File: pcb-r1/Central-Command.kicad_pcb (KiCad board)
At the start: 4 copper layers, 38.1 x 63.5 mm, 50 parts, among them P101 CONN_01X10, P102 CONN_01X10, P103 CONN_01X04, P104 CONN_01X02, P105 CONN_01X04, P106 CONN_01X02, P201 CONN_01X06, P202 CONN_01X04, P203 CONN_01X04, P204 CONN_01X03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

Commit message: Intermediate save of the layout
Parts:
- added C104: 0.1μF, Capacitors_SMD:C_0805, B.Cu at (93.5, 90.6)
- added C105: 1μF, Capacitors_SMD:C_1206, B.Cu at (95.8, 90.0)
- added C106: 10μF, Capacitors_SMD:C_1206, B.Cu at (98.3, 90.0)
- added C107: 0.1μF, Capacitors_SMD:C_0805, B.Cu at (98.3, 106.6)
- added C108: 1μF, Capacitors_SMD:C_1206, B.Cu at (95.9, 107.1)
- added C109: 10μF, Capacitors_SMD:C_1206, B.Cu at (93.4, 107.1)
- added R206: 0Ω, Resistors_SMD:R_0805, B.Cu at (81.9, 117.3)
- added R207: 0Ω, Resistors_SMD:R_0805, B.Cu at (81.9, 115.2)
- added R208: 0Ω, Resistors_SMD:R_0805, B.Cu at (81.9, 113.0)
- added R209: 0Ω, Resistors_SMD:R_0805, B.Cu at (81.9, 110.9)
- C101, C102, C103, C201, C301, C304, C305, C306, R201, R202, R203, R204, R205, R301, R302, R303, R304, R305, R306, R307: moved to B.Cu
- P302: value CONN_01X02 -> ALT PWR
- moved P205 32.6 mm to (112.1, 118.1)
- moved R303 21.5 mm to (82.2, 122.9), turned to 270 degrees
- moved R302 21.5 mm to (79.8, 122.9), turned to 270 degrees
- moved P302 17.1 mm to (96.8, 137.7), turned to 90 degrees
- moved R205 16.4 mm to (108.5, 118.1), turned to 0 degrees
- moved C301 13.6 mm to (83.6, 132.1), turned to 0 degrees
- moved D301 13.0 mm to (98.8, 133.3), turned to 0 degrees
- moved P105 12.6 mm to (112.1, 124.3)
- moved P202 12.5 mm to (84.6, 117.5)
- moved R301 12.4 mm to (90.4, 118.9), turned to 90 degrees
- moved P104 11.7 mm to (112.1, 111.9)
- moved C103 11.2 mm to (83.4, 91.1), turned to 0 degrees
- moved L101 10.4 mm to (90.8, 92.7), turned to 225 degrees
- moved C201 9.51 mm to (95.2, 116.1)
- moved R307 8.87 mm to (93.3, 125.6)
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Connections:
- net Net-(C302-Pad1) renamed /Power/VCCIO
- P103 pad 3: (no net) -> /SPI_MISO
- P103 pad 4: (no net) -> /SPI_MOSI
- P104 pad 2: (no net) -> /I2C1_SCK
- P203 pad 1: /Comm/SDA -> Net-(P203-Pad1)
- P203 pad 2: /Comm/SCL -> Net-(P203-Pad2)
- P203 pad 3: /Comm/PWR -> Net-(P203-Pad3)
- P203 pad 4: GND -> Net-(P203-Pad4)
- P301 pad 4: (no net) -> Net-(P301-Pad4)
- R204 pad 1: (no net) -> /Comm/TRACE
- R301 pad 2: (no net) -> /Comm/NRST
- SW201 pad 2: /Comm/NRST -> GND
- U101 pad 36: (no net) -> /I2C1_SCK
- U101 pad 40: (no net) -> /SPI1_MISO
- U101 pad 41: (no net) -> /SPI1_MOSI
- U301 pad 10: (no net) -> Net-(U301-Pad10)
- U301 pad 11: (no net) -> Net-(U301-Pad11)
- U301 pad 12: (no net) -> Net-(U301-Pad12)
- U301 pad 13: (no net) -> Net-(U301-Pad13)
- U301 pad 23: (no net) -> Net-(U301-Pad23)
- U301 pad 25: (no net) -> Net-(U301-Pad25)
- U301 pad 27: (no net) -> Net-(U301-Pad27)
- U301 pad 28: (no net) -> Net-(U301-Pad28)
- U301 pad 29: (no net) -> Net-(U301-Pad29)
- U301 pad 3: (no net) -> Net-(U301-Pad3)
- U301 pad 31: (no net) -> Net-(U301-Pad31)
- U301 pad 33: (no net) -> GND
- U301 pad 5: (no net) -> Net-(U301-Pad5)
- U301 pad 6: (no net) -> Net-(U301-Pad6)
- U301 pad 7: (no net) -> Net-(U301-Pad7)
- U301 pad 9: (no net) -> Net-(U301-Pad9)
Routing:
- net GND: track 0.00 -> 89.0 mm, vias 0 -> 15
- net /Power/VCCIO: track 0.00 -> 43.9 mm, vias 0 -> 3
- net /Comm/PWR: track 0.00 -> 37.7 mm, vias 0 -> 6
- net Net-(C305-Pad1): track 0.00 -> 21.5 mm, vias 0 -> 1
- net /Comm/BOOT0: track 0.00 -> 15.0 mm
- net Net-(P301-Pad2): track 0.00 -> 13.3 mm
- net Net-(R301-Pad1): track 0.00 -> 9.33 mm, vias 0 -> 1
- net Net-(C301-Pad1): track 0.00 -> 8.57 mm, vias 0 -> 1
- net Net-(P301-Pad3): track 0.00 -> 8.32 mm
- net Net-(C101-Pad1): track 0.00 -> 7.80 mm, vias 0 -> 1
- net Net-(D301-Pad2): track 0.00 -> 7.18 mm
- net /Comm/NRST: track 0.00 -> 6.92 mm, vias 0 -> 1
- net Net-(R305-Pad2): track 0.00 -> 4.84 mm, vias 0 -> 1
- net Net-(C304-Pad1): track 0.00 -> 3.87 mm, vias 0 -> 1
- net Net-(R304-Pad2): track 0.00 -> 3.53 mm, vias 0 -> 1
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- added copper zone on PWR, net /Comm/PWR
- added copper zone on GND, net GND

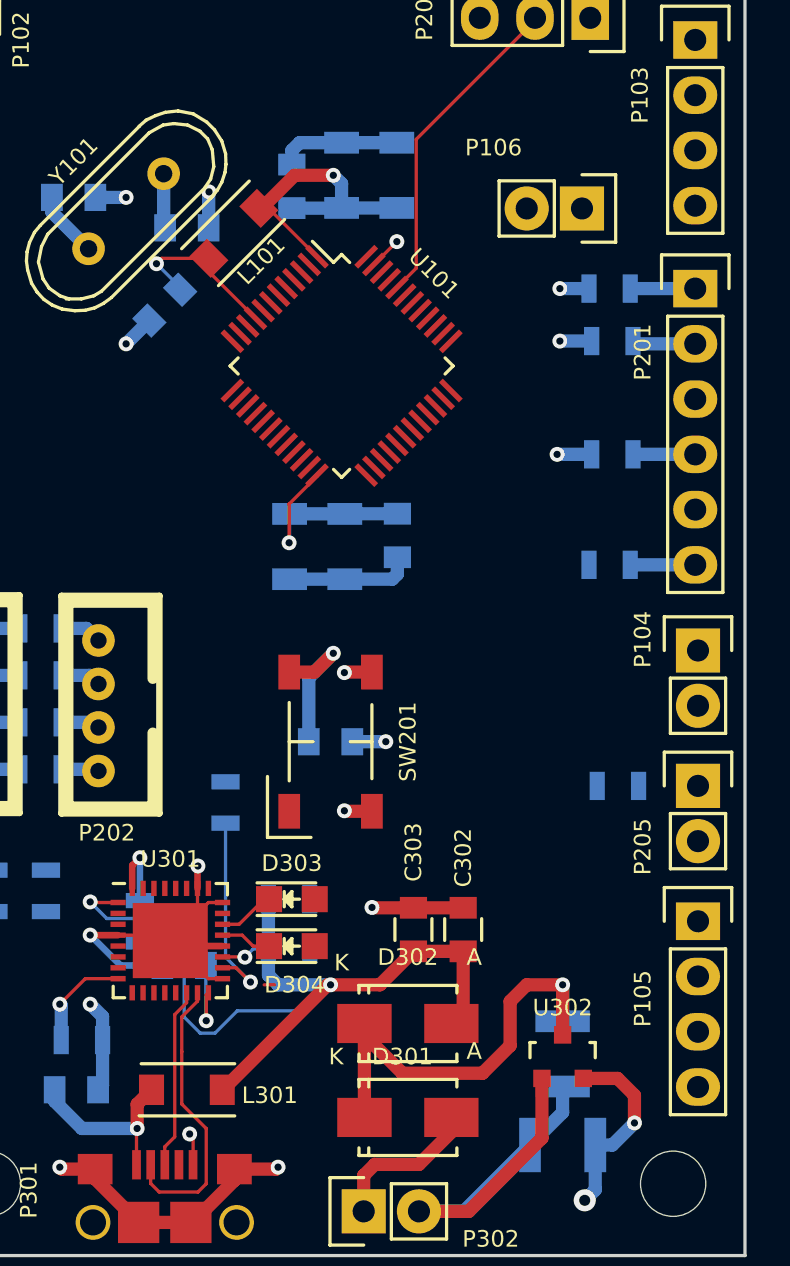
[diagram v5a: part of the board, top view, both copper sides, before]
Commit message: Started the basic layout.
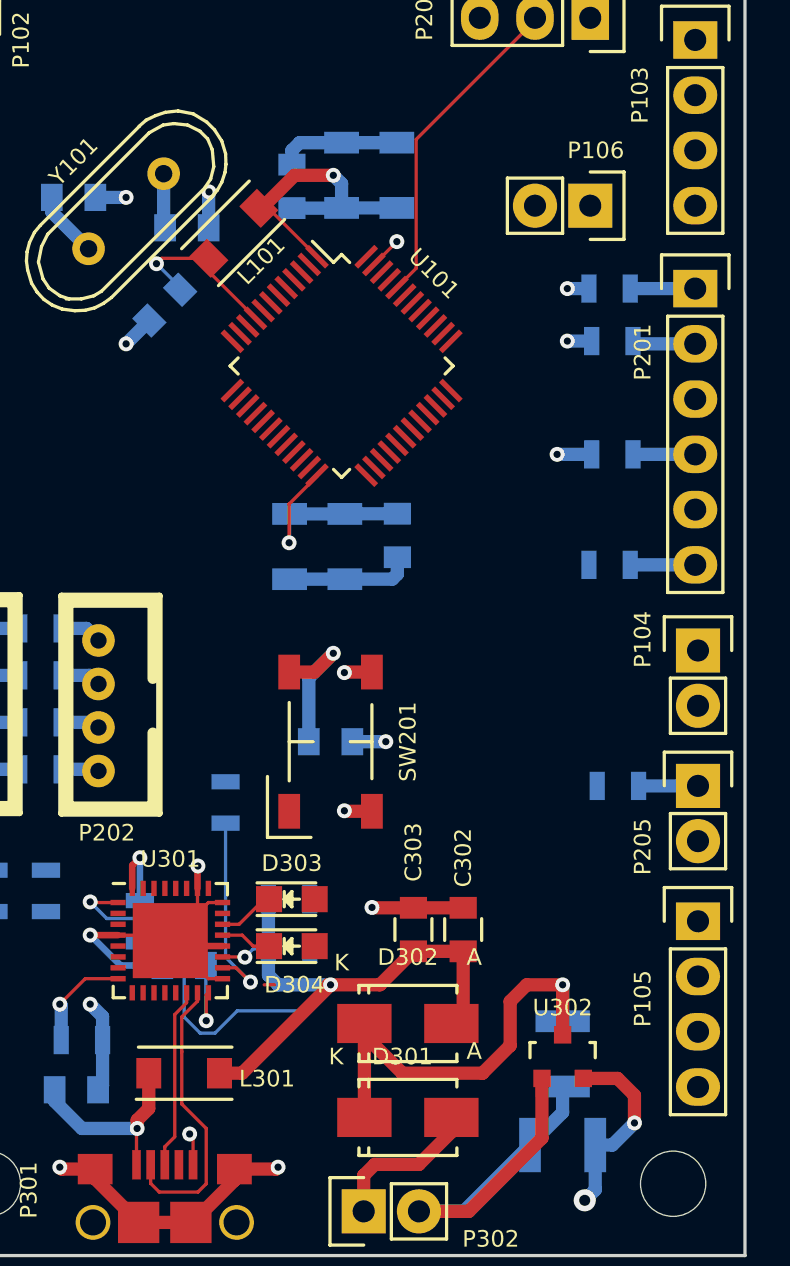
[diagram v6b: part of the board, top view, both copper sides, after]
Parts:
- moved L301 0.77 mm to (88.5, 131.3)
- moved P106 0.40 mm to (107.2, 91.4)
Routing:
- net Net-(P205-Pad1): track 0.00 -> 2.73 mm
- net Net-(C301-Pad1): track 8.57 -> 9.28 mm
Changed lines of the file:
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@@
   (general
     (links 145)
-    (no_connects 55)
-    (area 76.124999 76.124999 114.375001 139.775001)
+    (no_connects 54)
+    (area 74.587101 74.3331 117.711947 142.14856)
     (thickness 1.6)
     (drawings 4)
-    (tracks 254)
+    (tracks 256)
     (zones 0)
     (modules 60)
@@
   )
   (setup
-    (last_trace_width 0.6096)
+    (last_trace_width 0.1524)
     (user_trace_width 0.3048)
     (user_trace_width 0.6096)
@@
   )
   (module Inductors_NEOSID:Neosid_Inductor_SM1206 (layer F.Cu)
-    (at 88.646 132.08)
+    (at 88.519 131.318)
     (descr "Neosid, Inductor, SM1206, Festinduktivitaet, SMD,")
     (tags "Neosid, Inductor, SM1206, Festinduktivitaet, SMD,")
@@
   )
   (module Pin_Headers:Pin_Header_Straight_1x02 (layer F.Cu)
-    (at 106.807 91.567 270)
+    (at 107.188 91.44 270)
     (descr "Through hole pin header")
     (tags "pin header")
-    (fp_text reference P106 (at -2.794 4.064 360) (layer F.SilkS)
+    (fp_text reference P106 (at -2.54 -0.254 360) (layer F.SilkS)
       (effects (font (size 0.762 0.762) (thickness 0.127)))
     )
@@
   (segment (start 89.655527 93.859473) (end 89.655527 94.471294) (width 0.1524) (layer F.Cu) (net 1))
   (segment (start 89.655527 94.471294) (end 91.798202 96.613969) (width 0.1524) (layer F.Cu) (net 1))
-  (segment (start 107.254 97.663) (end 105.791 97.663) (width 0.6096) (layer B.Cu) (net 2) (status 400000))
-  (via (at 105.791 97.663) (size 0.6858) (drill 0.3302) (layers F.Cu B.Cu) (net 2))
+  (via (at 106.133919 97.663) (size 0.6858) (drill 0.3302) (layers F.Cu B.Cu) (net 2))
+  (segment (start 107.254 97.663) (end 106.133919 97.663) (width 0.6096) (layer B.Cu) (net 2))
   (segment (start 96.25 116.078) (end 97.79 116.078) (width 0.6096) (layer B.Cu) (net 2))
   (via (at 97.79 116.078) (size 0.6858) (drill 0.3302) (layers F.Cu B.Cu) (net 2))
@@
   (via (at 95.377 112.014) (size 0.6858) (drill 0.3302) (layers F.Cu B.Cu) (net 5))
   (segment (start 94.25 113.141) (end 95.377 112.014) (width 0.6096) (layer B.Cu) (net 5))
+  (segment (start 86.36 133.858) (end 86.36 133.477) (width 0.6096) (layer F.Cu) (net 6))
+  (segment (start 86.8934 132.9436) (end 86.8934 131.318) (width 0.6096) (layer F.Cu) (net 6))
+  (segment (start 86.36 133.477) (end 86.8934 132.9436) (width 0.6096) (layer F.Cu) (net 6))
   (segment (start 82.566 132.08) (end 82.566 132.604) (width 0.6096) (layer B.Cu) (net 6))
   (segment (start 82.566 132.604) (end 83.82 133.858) (width 0.6096) (layer B.Cu) (net 6))
   (segment (start 83.82 133.858) (end 86.36 133.858) (width 0.6096) (layer B.Cu) (net 6))
   (via (at 86.36 133.858) (size 0.6858) (drill 0.3302) (layers F.Cu B.Cu) (net 6))
-  (segment (start 86.36 133.858) (end 86.36 132.7404) (width 0.6096) (layer F.Cu) (net 6))
-  (segment (start 86.36 132.7404) (end 87.0204 132.08) (width 0.6096) (layer F.Cu) (net 6))
   (segment (start 86.33 133.888) (end 86.33 135.526) (width 0.1524) (layer F.Cu) (net 6))
   (segment (start 86.36 133.858) (end 86.33 133.888) (width 0.1524) (layer F.Cu) (net 6))
@@
   (via (at 105.918 127.254) (size 0.6858) (drill 0.3302) (layers F.Cu B.Cu) (net 8))
   (segment (start 96.80702 133.35) (end 96.80702 129.032) (width 0.6096) (layer F.Cu) (net 8))
-  (segment (start 107.254 102.87) (end 105.664 102.87) (width 0.6096) (layer B.Cu) (net 9) (status 400000))
+  (via (at 106.133919 95.25) (size 0.6858) (drill 0.3302) (layers F.Cu B.Cu) (net 9))
+  (segment (start 107.127 95.25) (end 106.133919 95.25) (width 0.6096) (layer B.Cu) (net 9))
+  (segment (start 107.254 102.87) (end 105.664 102.87) (width 0.6096) (layer B.Cu) (net 9))
   (via (at 105.664 102.87) (size 0.6858) (drill 0.3302) (layers F.Cu B.Cu) (net 9))
   (segment (start 91.954473 91.560527) (end 92.081473 91.560527) (width 0.6096) (layer F.Cu) (net 9))
@@
   (segment (start 91.954473 91.560527) (end 92.401614 91.560527) (width 0.1524) (layer F.Cu) (net 9))
   (segment (start 92.401614 91.560527) (end 94.626629 93.785542) (width 0.1524) (layer F.Cu) (net 9))
-  (segment (start 107.127 95.25) (end 105.791 95.25) (width 0.6096) (layer B.Cu) (net 9))
-  (via (at 105.791 95.25) (size 0.6858) (drill 0.3302) (layers F.Cu B.Cu) (net 9))
   (segment (start 82.865 115.189) (end 84.346 115.189) (width 0.6096) (layer B.Cu) (net 9))
   (segment (start 84.346 115.189) (end 84.582 115.425) (width 0.6096) (layer B.Cu) (net 9))
@@
   (segment (start 112.014 97.79) (end 109.281 97.79) (width 0.6096) (layer B.Cu) (net 44))
   (segment (start 109.281 97.79) (end 109.154 97.663) (width 0.6096) (layer B.Cu) (net 44))
-  (segment (start 112.014 102.87) (end 109.154 102.87) (width 0.6096) (layer B.Cu) (net 45) (status C00000))
-  (segment (start 112.014 107.95) (end 109.027 107.95) (width 0.6096) (layer B.Cu) (net 46) (status C00000))
+  (segment (start 112.014 102.87) (end 109.154 102.87) (width 0.6096) (layer B.Cu) (net 45))
+  (segment (start 112.014 107.95) (end 109.027 107.95) (width 0.6096) (layer B.Cu) (net 46))
   (segment (start 82.865 113.03) (end 84.187 113.03) (width 0.6096) (layer B.Cu) (net 47))
   (segment (start 84.187 113.03) (end 84.582 113.425) (width 0.6096) (layer B.Cu) (net 47))
@@
   (segment (start 99.187 88.392) (end 99.187 94.316339) (width 0.1524) (layer F.Cu) (net 49))
   (segment (start 99.187 94.316339) (end 98.303584 95.199755) (width 0.1524) (layer F.Cu) (net 49))
+  (segment (start 112.141 118.11) (end 109.408 118.11) (width 0.6096) (layer B.Cu) (net 50))
   (segment (start 88.087189 134.241411) (end 87.63 134.6986) (width 0.1524) (layer F.Cu) (net 51))
   (segment (start 88.634 127.622) (end 88.634 128.076452) (width 0.1524) (layer F.Cu) (net 51))
@@
   (via (at 82.804 128.143) (size 0.6858) (drill 0.3302) (layers F.Cu B.Cu) (net 59))
   (segment (start 82.87 128.209) (end 82.804 128.143) (width 0.6096) (layer B.Cu) (net 59))
+  (segment (start 90.1446 131.318) (end 91.186 131.318) (width 0.6096) (layer F.Cu) (net 81))
+  (segment (start 91.186 131.318) (end 95.25 127.254) (width 0.6096) (layer F.Cu) (net 81))
   (segment (start 94.056191 128.447809) (end 94.907101 127.596899) (width 0.1524) (layer B.Cu) (net 81))
   (segment (start 90.965015 128.447809) (end 94.056191 128.447809) (width 0.1524) (layer B.Cu) (net 81))
@@
   (segment (start 92.395 126.812) (end 92.837 127.254) (width 0.6096) (layer B.Cu) (net 81))
   (segment (start 92.395 123.317) (end 92.395 125.603) (width 0.6096) (layer B.Cu) (net 81))
-  (segment (start 90.2716 132.08) (end 90.297 132.08) (width 0.6096) (layer F.Cu) (net 81))
-  (segment (start 90.297 132.08) (end 95.123 127.254) (width 0.6096) (layer F.Cu) (net 81))
   (segment (start 95.123 127.254) (end 97.52 127.254) (width 0.6096) (layer F.Cu) (net 81))
   (segment (start 97.52 127.254) (end 99.06 125.714) (width 0.6096) (layer F.Cu) (net 81))

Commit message: Final draft layout. Published to build log as V01
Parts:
- C302, C303: moved to B.Cu
- R208, R209: moved to F.Cu
- moved P101 58.8 mm to (112.0, 129.9), turned to 180 degrees
- moved P202 38.0 mm to (111.4, 90.6)
- moved P105 33.7 mm to (78.7, 128.9), turned to 180 degrees
- moved P201 32.2 mm to (84.3, 78.7), turned to 90 degrees
- moved R205 29.4 mm to (82.2, 104.9)
- moved P205 29.1 mm to (85.6, 106.3), turned to 135 degrees
- moved R204 27.8 mm to (97.0, 82.4), turned to 90 degrees
- moved R208 27.1 mm to (90.6, 87.3)
- moved R209 27.1 mm to (90.6, 85.2)
- moved R203 27.0 mm to (84.3, 82.4), turned to 270 degrees
- moved R207 27.0 mm to (84.8, 88.4)
- moved R206 26.9 mm to (84.8, 90.6)
- moved P203 26.8 mm to (79.9, 84.5)
- moved R202 26.3 mm to (86.7, 82.4), turned to 90 degrees
- moved R201 26.1 mm to (91.9, 82.4), turned to 270 degrees
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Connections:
- P103 pad 3: /SPI_MISO -> /SPI1_MISO
- P103 pad 4: /SPI_MOSI -> /SPI1_MOSI
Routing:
- net /Comm/SWCLK: track 2.91 -> 61.5 mm, vias 0 -> 1
- net /Comm/NRST: track 6.92 -> 64.3 mm, vias 1 -> 2
- net /Comm/SWIO: track 2.86 -> 57.9 mm, vias 0 -> 1
- net /Comm/SDA: track 1.95 -> 46.9 mm, vias 0 -> 1
- net /Comm/SCL: track 1.88 -> 45.6 mm, vias 0 -> 1
- net /ADC_IN1: track 0.00 -> 35.2 mm, vias 0 -> 1
- net Net-(P101-Pad3): track 0.00 -> 34.0 mm
- net Net-(P101-Pad4): track 0.00 -> 32.8 mm, vias 0 -> 1
- net /ADC_IN8: track 0.00 -> 32.2 mm, vias 0 -> 2
- net Net-(P101-Pad1): track 0.00 -> 28.8 mm, vias 0 -> 1
- net Net-(P101-Pad5): track 0.00 -> 28.3 mm
- net Net-(P101-Pad2): track 0.00 -> 26.6 mm, vias 0 -> 1
- net Net-(P101-Pad6): track 0.00 -> 25.1 mm
- net /Comm/MCO: track 0.00 -> 25.0 mm, vias 0 -> 1
- net /ADC_IN9: track 0.00 -> 24.9 mm
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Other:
- board text added: "+"
- board text added: "A"
- board text added: "Alt PWR"
- board text added: "Central Command Module Rev 4L.1"
- board text added: "GND A-IN9 A-IN8 A-IN1"
- board text added: "I2C Input"
- board text added: "I2C Ouput"
- board text added: "MCO GND"
- board text added: "PB15 PB14 PB13 PB12 PB11 PB10 PB8 PB2 PA10 PA9"
- board text added: "PC13 PC14 PC15 PB9 MCO PA0 PA4 PA5 PA6 PA7"
- board text added: "PWR BOOT GND"
- board text added: "PWR SWC GND SWI ~RST~ TRC"
- board text added: "RESET"
- board text added: "Rx"
- board text added: "Rx Tx"
- board text added: "SDA SCK"
- board text added: "SDA SCK I2C1"
- board text added: "SDA SCL PWR GND"
- board text added: "SPI1 MOSI MISO CSK ~SS"
- board text added: "Tx"

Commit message: Completed the layout. Saving before sending off to Fab.
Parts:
- removed P205: CONN_01X02, Pin_Headers:Pin_Header_Straight_1x02
- removed R205: R, Resistors_SMD:R_0805
- D303: value LED -> Tx LED
- D304: value LED -> Rx LED
- R208, R209: moved to B.Cu
- moved P202 32.2 mm to (79.8, 84.3), turned to 270 degrees
- moved P203 31.5 mm to (110.9, 90.3), turned to 90 degrees
- moved R206 20.1 mm to (103.4, 82.9), turned to 180 degrees
- moved R207 18.9 mm to (103.4, 85.1), turned to 180 degrees
- moved R209 13.4 mm to (103.4, 89.4), turned to 180 degrees
- moved R208 12.8 mm to (103.4, 87.2), turned to 180 degrees
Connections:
- P101 pad 10: Net-(P101-Pad10) -> /PA10
- P101 pad 8: Net-(P101-Pad8) -> /MCO
- P101 pad 9: Net-(P101-Pad9) -> /PA9
- P102 pad 5: /Comm/MCO -> /PB8
- U101 pad 20: Net-(P101-Pad3) -> Net-(P101-Pad1)
- U101 pad 21: Net-(P101-Pad5) -> Net-(P101-Pad2)
- U101 pad 22: Net-(P101-Pad6) -> Net-(P101-Pad3)
- U101 pad 25: Net-(P101-Pad7) -> Net-(P101-Pad4)
- U101 pad 26: Net-(P101-Pad8) -> Net-(P101-Pad5)
- U101 pad 27: Net-(P101-Pad9) -> Net-(P101-Pad6)
- U101 pad 28: Net-(P101-Pad10) -> Net-(P101-Pad7)
- U101 pad 29: /Comm/MCO -> /MCO
- U101 pad 30: Net-(P101-Pad1) -> /PA9
- U101 pad 31: Net-(P101-Pad2) -> /PA10
- U101 pad 45: Net-(P101-Pad4) -> /PB8
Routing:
- net /PB8: track 0.00 -> 25.2 mm, vias 0 -> 1
- net /Comm/MCO: track 25.0 -> 0.00 mm, vias 1 -> 0
- net Net-(P101-Pad8): track 16.0 -> 0.00 mm
- net /MCO: track 0.00 -> 14.0 mm
- net Net-(P101-Pad9): track 13.4 -> 0.00 mm
- net Net-(P101-Pad10): track 13.1 -> 0.00 mm
- net /PA9: track 0.00 -> 12.7 mm
- net GND: track 97.2 -> 109.4 mm
- net /PA10: track 0.00 -> 11.6 mm
- net Net-(P101-Pad4): track 32.8 -> 23.2 mm, vias 1 -> 0
- net Net-(P101-Pad1): track 28.8 -> 37.5 mm, vias 1 -> 0
- net Net-(P205-Pad1): track 8.52 -> 0.00 mm
- net Net-(P101-Pad2): track 26.6 -> 34.5 mm, vias 1 -> 0
- net Net-(P101-Pad5): track 28.3 -> 20.4 mm
- net Net-(P101-Pad6): track 25.1 -> 18.4 mm
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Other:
- board text added: "A10 A9 MCO B15 B14 B13 B12 B11 B10 B2"
- board text added: "C13 C14 C15 B9 B8 A0 A4 A5 A6 A7"
- board text added: "GPIO Header 1"
- board text added: "GPIO Header 2"
- board text added: "MOSI MISO CSK ~SS"
- board text added: "Programming"
- board text added: "SPI1"
- board text added: "Sensor I2C"
- board text added: "UART"
- board text removed: "MCO GND"
- board text removed: "PB15 PB14 PB13 PB12 PB11 PB10 PB8 PB2 PA10 PA9"
- board text removed: "PC13 PC14 PC15 PB9 MCO PA0 PA4 PA5 PA6 PA7"
- board text removed: "SDA SCK I2C1"
- board text removed: "SPI1 MOSI MISO CSK ~SS"
